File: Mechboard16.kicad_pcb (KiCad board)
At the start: 2 copper layers, 386.1 x 97 mm, 269 parts, among them CN1 CONN_C16, CN2 CONN_+4, CN3 CONN_CLOCK, J201 USB_B, J202 CONN_ICSP, J203 CONN_MRESET, J204 CONN_LED, Q1 BSS138, Q2 BSS138, Q201 MMBT3904, Q202 MMBT3904, SW0:0 KEY_DEL, SW0:1 KEY_RET, SW0:2 KEY_PND, SW0:3 KEY_HLP, SW0:4 KEY_F1, SW0:5 KEY_F2, SW0:6 KEY_F3, SW0:7 KEY_AT, SW1:0 KEY_3, SW1:1 KEY_W, SW1:2 KEY_A, SW1:3 KEY_4, SW1:4 KEY_Z, SW1:5 KEY_S, SW1:6 KEY_E, SW1:7 KEY_LSH, SW1B:7 KEY_RSH, SW1C:7 KEY_CLK, SW201 SW_RESET, SW2:0 KEY_5, SW2:1 KEY_R, SW2:2 KEY_D, SW2:3 KEY_6, SW2:4 KEY_C, SW2:5 KEY_F, SW2:6 KEY_T, SW2:7 KEY_X, SW3:0 KEY_7, SW3:1 KEY_Y, SW3:2 KEY_G, SW3:3 KEY_8, SW3:4 KEY_B, SW3:5 KEY_H, SW3:6 KEY_U, SW3:7 KEY_V, SW4:0 KEY_9, SW4:1 KEY_I, SW4:2 KEY_J, SW4:3 KEY_0, SW4:4 KEY_M, SW4:5 KEY_K, SW4:6 KEY_O, SW4:7 KEY_N, SW5:0 KEY_DN, SW5:1 KEY_P, SW5:2 KEY_L, SW5:3 KEY_UP, SW5:4 KEY_DOT, SW5:5 KEY_COL, SW5:6 KEY_MIN, SW5:7 KEY_COM, SW6:0 KEY_LF, SW6:1 KEY_AST, SW6:2 KEY_SEM, SW6:3 KEY_RT, SW6:4 KEY_ESC, SW6:5 KEY_EQ, SW6:6 KEY_PLS, SW6:7 KEY_SLA, SW7:0 KEY_1, SW7:1 KEY_CLR, SW7:2 KEY_CTL, SW7:3 KEY_2, SW7:4 KEY_SPC, SW7:5 KEY_CMD, SW7:6 KEY_Q, SW7:7 KEY_RUN, U1 4066, U2 NE555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

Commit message: Some THT components -> SMD
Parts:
- C204, C4: footprint Capacitor_THT:CP_Radial_D5.0mm_P2.00mm -> Capacitor_SMD:C_1206_3216Metric_Pad1.33x1.80mm_HandSolder
- D201: footprint Diode_SMD:D_SMA -> Diode_SMD:D_SOD-323_HandSoldering
- moved C4 1.89 mm to (67.7, 115.1), turned to 270 degrees
- moved C204 1.56 mm to (397.6, 83.8)
- moved D201 0.75 mm to (399.5, 69.0)
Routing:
- net Net-(C4-Pad1): track 90.9 -> 88.6 mm
- net GND: track 499.6 -> 497.7 mm
- net +5V: track 693.5 -> 692.0 mm

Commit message: Preparing for PCBA
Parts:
- D201: value 1n5819 -> 1n4148
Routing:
- net col5: track 519.8 -> 523.2 mm
- net /USB Controller/lcol3: track 379.8 -> 381.1 mm
- net /USB Controller/lcol2: track 406.7 -> 407.5 mm
- net /USB Controller/lrow2: track 398.1 -> 398.7 mm

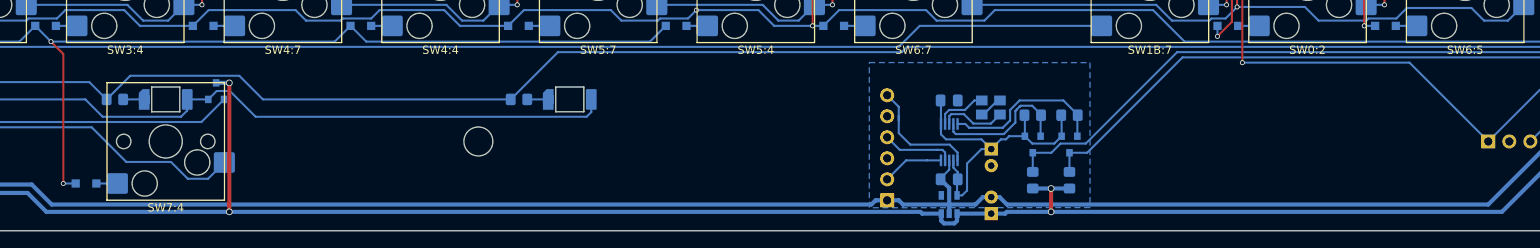
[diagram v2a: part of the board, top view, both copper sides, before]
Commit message: Slight reword in clock generator area
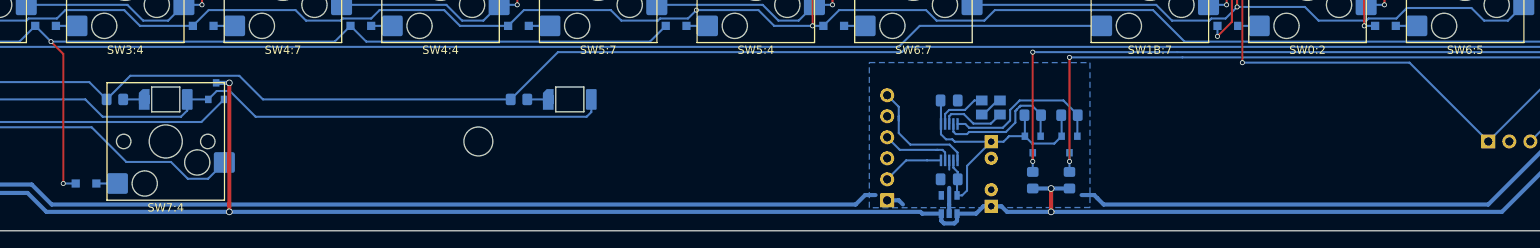
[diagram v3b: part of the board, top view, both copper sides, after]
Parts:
- moved C8 0.89 mm to (262.0, 114.3)
- moved C7 0.89 mm to (262.0, 122.1)
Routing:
- net GND: track 497.7 -> 471.8 mm
- net /USB Controller/soft_i2c_scl: track 134.1 -> 142.4 mm, vias 2 -> 4
- net /USB Controller/soft_i2c_sda: track 130.0 -> 137.8 mm, vias 2 -> 4
- net +5V: track 692.0 -> 692.7 mm
- net +3V3: track 38.3 -> 37.7 mm

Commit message: Add ROM switcher
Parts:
- added CN4: CONN_ROMSWITCH, Connector_PinHeader_2.54mm:PinHeader_1x03_P2.54mm_Vertical, B.Cu at (50.0, 115.7)
- added R5: 10k, Resistor_SMD:R_0805_2012Metric_Pad1.20x1.40mm_HandSolder, B.Cu at (54.6, 120.0)
- moved C1 2.54 mm to (61.9, 119.5)
- moved C3 2.54 mm to (61.9, 110.6)
- moved R1 2.54 mm to (54.6, 117.0)
- moved R3 2.54 mm to (54.6, 110.6)
- moved R4 2.54 mm to (54.6, 113.8)
- moved U2 2.54 mm to (61.9, 115.1)
- moved C4 2.54 mm to (70.2, 115.1)
- moved R2 2.54 mm to (69.2, 110.6)
- renumbered R5 to R6, R6 to R7, R7 to R8, R8 to R9
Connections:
- U1 pad 11: Net-(U1-Pad11) -> Net-(CN4-Pad2)
- U1 pad 12: GND -> /USB Controller/~switch
- U1 pad 3: Net-(U1-Pad3) -> /USB Controller/~switch
- U1 pad 4: Net-(U1-Pad4) -> GND
- U1 pad 5: GND -> ROM_SWITCH
- U1 pad 6: GND -> ROM_SWITCH
- U1 pad 8: Net-(U1-Pad8) -> Net-(CN4-Pad2)
- U201 pad 1: Net-(U201-Pad1) -> ROM_SWITCH
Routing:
- net ROM_SWITCH: track 0.00 -> 399.1 mm, vias 0 -> 4
- net /USB Controller/~switch: track 0.00 -> 14.8 mm, vias 0 -> 2
- net Net-(JP2-Pad1): track 73.6 -> 87.7 mm
- net Net-(CN4-Pad2): track 0.00 -> 10.1 mm
- net Net-(CN4-Pad1): track 0.00 -> 8.62 mm
- net +5V: track 692.7 -> 700.2 mm
- net Net-(C4-Pad1): track 88.6 -> 92.9 mm
- net row1: track 577.1 -> 573.3 mm
- net GND: track 471.8 -> 468.2 mm
- net Net-(CN4-Pad3): track 0.00 -> 3.39 mm
- net Net-(R2-Pad2): track 28.1 -> 30.7 mm
- net /USB Controller/lcol1: track 365.8 -> 363.5 mm
- net col3: track 416.1 -> 414.2 mm
- net /USB Controller/~reset: track 40.2 -> 40.7 mm
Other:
- board text added: "COMMODORE 16/LITTLESIXTEEN"
- board text added: "SHIFT LOCK LATCH & ROM SWITCHER"
- board text removed: "COMMODORE 16"
- board text removed: "SHIFT LOCK CIRCUIT"

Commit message: Add series resistors on clock outputs
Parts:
- added R10: 0, Resistor_SMD:R_0805_2012Metric_Pad1.20x1.40mm_HandSolder, B.Cu at (255.9, 119.0)
- added R11: 47, Resistor_SMD:R_0805_2012Metric_Pad1.20x1.40mm_HandSolder, B.Cu at (255.9, 114.4)
- added R12: 100, Resistor_SMD:R_0805_2012Metric_Pad1.20x1.40mm_HandSolder, B.Cu at (255.9, 109.9)
- moved C5 2.54 mm to (259.5, 118.9)
- moved C6 2.54 mm to (259.5, 109.3)
- moved C7 2.54 mm to (264.5, 122.1)
- moved C8 2.54 mm to (264.5, 114.3)
- moved Q1 2.54 mm to (274.0, 114.7)
- moved Q2 2.54 mm to (269.6, 114.7)
- moved R6 2.54 mm to (269.6, 119.0)
- moved R7 2.54 mm to (274.0, 119.0)
- moved R8 2.54 mm to (269.6, 111.1)
- moved R9 2.54 mm to (274.0, 111.1)
- moved U3 2.54 mm to (259.5, 114.4)
- moved U4 2.54 mm to (259.5, 121.9)
- moved Y1 2.54 mm to (264.5, 110.2)
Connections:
- U3 pad 10: /USB Controller/clk0 -> Net-(R10-Pad2)
- U3 pad 6: /USB Controller/clk2 -> Net-(R12-Pad2)
- U3 pad 9: /USB Controller/clk1 -> Net-(R11-Pad2)
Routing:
- net Net-(R12-Pad2): track 0.00 -> 8.60 mm
- net /USB Controller/clk2: track 14.7 -> 6.54 mm
- net GND: track 468.2 -> 463.3 mm
- net Net-(R11-Pad2): track 0.00 -> 4.09 mm
- net Net-(R10-Pad2): track 0.00 -> 3.65 mm
- net /USB Controller/soft_i2c_sda: track 137.8 -> 135.3 mm
- net /USB Controller/soft_i2c_scl: track 142.3 -> 139.8 mm
- net /USB Controller/clk1: track 8.84 -> 6.62 mm
- net /USB Controller/clk0: track 7.45 -> 6.94 mm

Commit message: Almost there
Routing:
- net /USB Controller/lcol7: track 461.5 -> 460.8 mm
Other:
- board text added: "METROPOLIS HAS NOTHING ON THIS"

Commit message: Ready for V2 RC1
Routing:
- net /USB Controller/lcol5: track 465.6 -> 469.1 mm
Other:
- board text added: "CC-BY-NC-SA © SukkoPera 2023-2026 Heavily inspired by MechBoard64 by MtnBuffalo github.com/SukkoPera/MechBoard16"
- board text added: "HALB WESEN UND ÜBER DING"
- board text added: "USB, LED, ROM & CLOCK CONTROLLER"
- board text removed: "CC-BY-NC-SA © SukkoPera 2023-2025 Heavily inspired by MechBoard64 by MtnBuffalo github.com/SukkoPera/MechBoard16"
- board text removed: "METROPOLIS HAS NOTHING ON THIS"
- board text removed: "USB, LED & CLOCK CONTROLLER"
